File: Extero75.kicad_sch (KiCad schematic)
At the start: 314 parts, among them J1 USB_C_Receptacle_USB2.0, Q1 AO3400A, SW1 BOOT, SW2 RST, SW3 RotaryEncoder_Switch, U1 STM32F072R8Tx, U2 XC6206P332MR

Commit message: change name
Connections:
- no-connect marks 2 -> 14
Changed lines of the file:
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@@
   (no_connect (at 641.858 63.246))
   (no_connect (at 641.858 60.706))
+  (no_connect (at 716.788 174.498))
+  (no_connect (at 716.788 154.178))
+  (no_connect (at 716.788 169.418))
+  (no_connect (at 716.788 156.718))
+  (no_connect (at 716.788 166.878))
+  (no_connect (at 716.788 151.638))
+  (no_connect (at 716.788 164.338))
+  (no_connect (at 716.788 161.798))
+  (no_connect (at 716.788 159.258))
+  (no_connect (at 716.788 171.958))
+  (no_connect (at 716.788 177.038))
+  (no_connect (at 716.788 179.578))
   (wire (pts (xy 516.636 204.343) (xy 512.318 204.343))
     (stroke (width 0) (type default) (color 0 0 0 0))

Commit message: some more routing
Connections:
- net +3V3 is gone; now on net +3.3V: C12.1, C13.1, C14.1, C15.1, C16.1, C8.1, C9.1, U2.2 (VO)
- net +5V: now also Tab1.4 (LEDGND)
- net COL10: no longer U1.5 (PF0)
- net COL11: no longer U1.6 (PF1)
- net COL12: no longer U1.14 (PA0)
- net COL13: no longer U1.28 (PB2)
- net COL14: no longer U1.29 (PB10)
- net COL15: no longer U1.30 (PB11)
- net COL16: no longer U1.8 (PC0)
- net COL17: no longer U1.9 (PC1)
- net COL4: now also U1.37 (PC6); no longer U1.41 (PA8)
- net COL5: now also U1.38 (PC7); no longer U1.43 (PA10)
- net COL6: now also U1.39 (PC8); no longer U1.46 (PA13)
- net COL7: now also U1.40 (PC9); no longer U1.49 (PA14)
- net COL8: no longer U1.62 (PB9)
- net COL9: now also MX-J1.1 (COL), MX-U1.1 (COL), Num7.1 (COL); no longer U1.54 (PD2)
- net D_N: now also U1.44 (PA11); no longer U1.26 (PB0)
- net D_P: now also U1.45 (PA12); no longer U1.27 (PB1)
- net LED-: now also R21.2
- net LED_PWM: no longer U1.42 (PA9)
- net ROTA: no longer U1.4 (PC15)
- net ROTB: no longer U1.3 (PC14)
- net ROW0: now also U1.41 (PA8); no longer U1.50 (PA15)
- net ROW1: now also U1.5 (PF0); no longer U1.56 (PB4)
- net ROW2: now also U1.6 (PF1); no longer U1.57 (PB5)
- net ROW3: now also U1.8 (PC0); no longer U1.58 (PB6)
- net ROW4: now also U1.9 (PC1); no longer U1.59 (PB7)
- net ROW5: now also U1.10 (PC2); no longer U1.61 (PB8)
- net at Num1.3 (LED): now also R25.1
- net BOOT: now reaches C1.1, R3.1, SW1.2, U1.60 (BOOT0)
- net RST: now reaches C2.1, SW2.2, U1.7 (NRST)
- net UGLED: no longer names the net of U1.55 (PB3)
- no-connect marks 14 -> 4
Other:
- note removed: "RESET"
- moved on the sheet: D15, R21, R25, Tab1

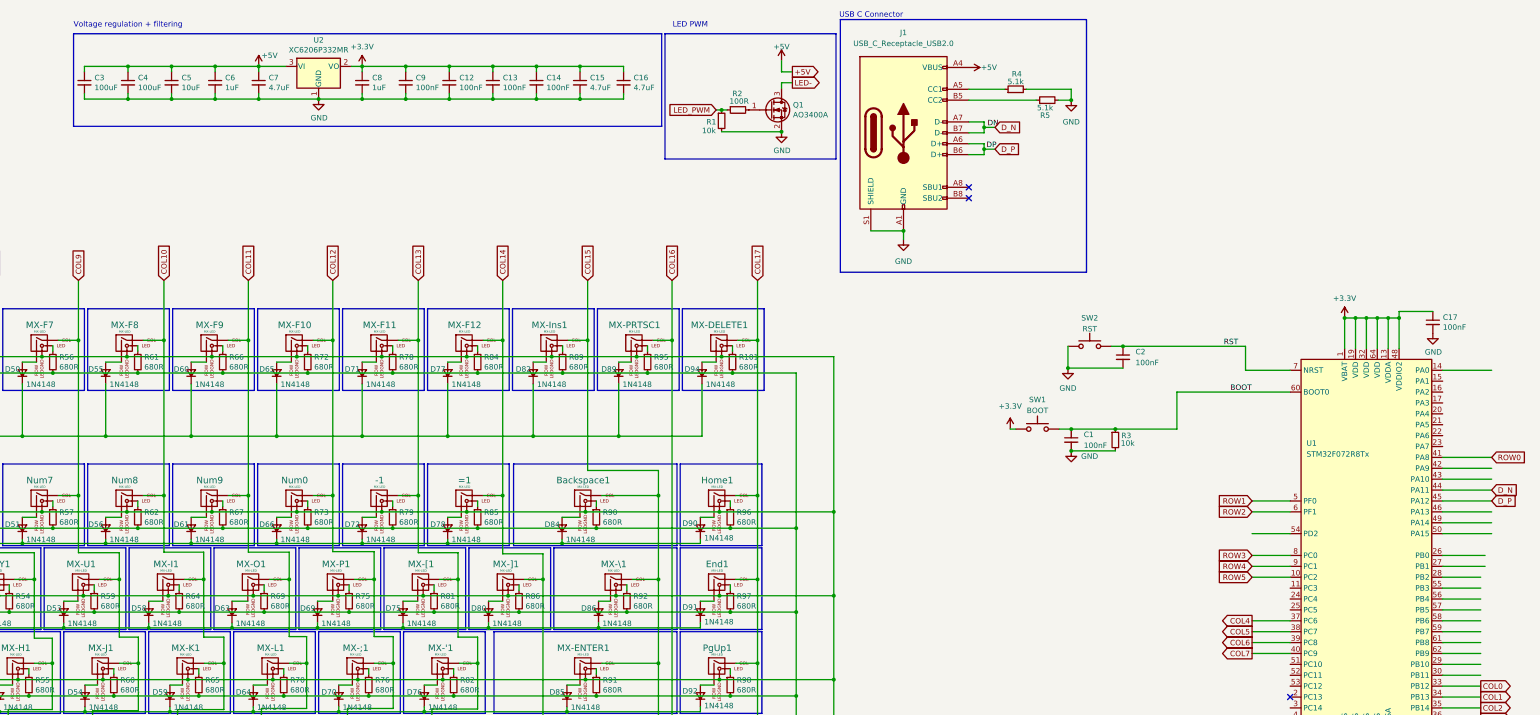
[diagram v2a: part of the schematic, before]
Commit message: Fix decoupling capacitor schematic for Voltage regulator + Some more routing
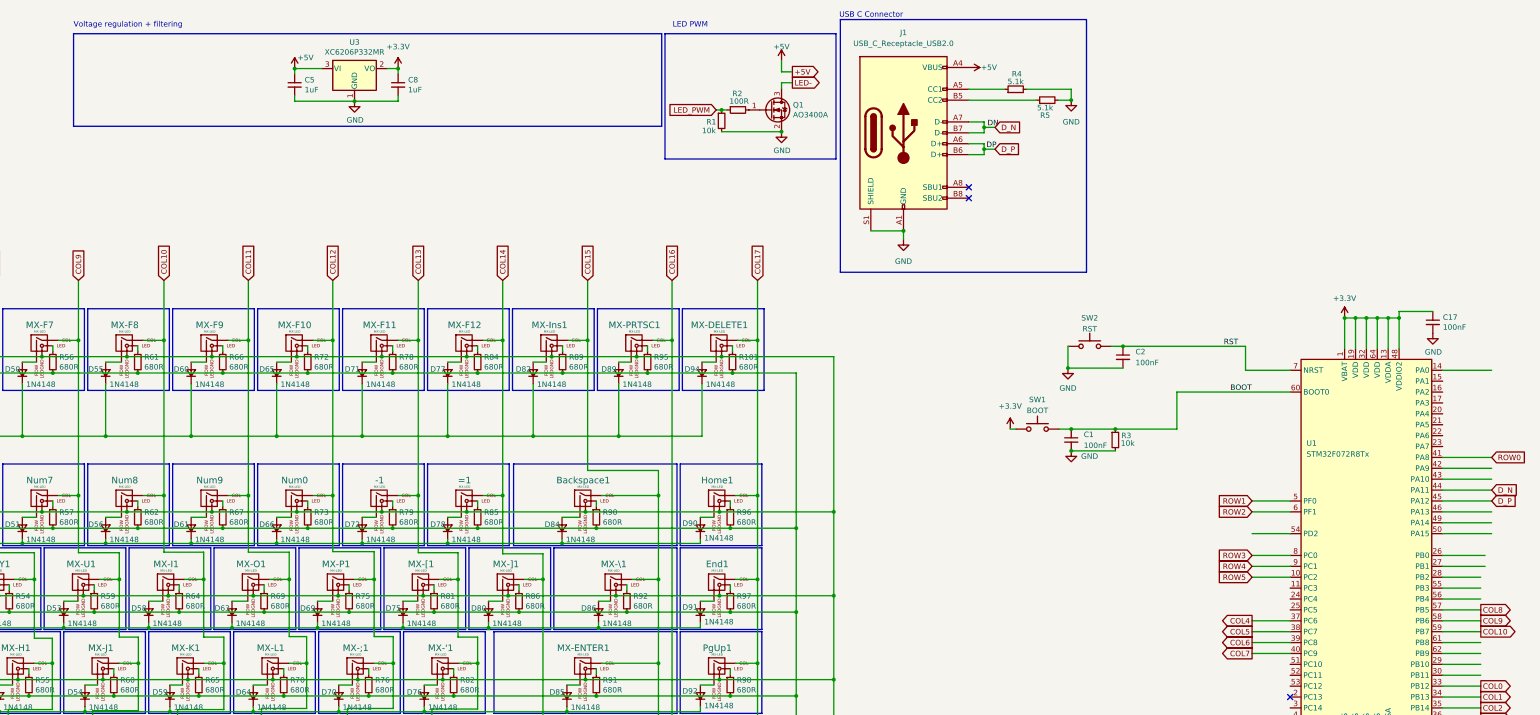
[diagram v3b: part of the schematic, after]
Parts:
- removed C12, C13, C14, C9: 100nF, Capacitor_SMD:C_0402_1005Metric, symbol Device:C_Small
- removed C15, C16, C7: 4.7uF, Capacitor_SMD:C_0402_1005Metric, symbol Device:C_Small
- removed C3, C4: 100uF, Capacitor_Tantalum_SMD:CP_EIA-3528-21_Kemet-B, symbol Device:C_Small
- removed C6: 1uF, Capacitor_SMD:C_0402_1005Metric, symbol Device:C_Small
- removed U2: XC6206P332MR, Package_TO_SOT_SMD:SOT-23, symbol isometria-75-pcb-iso-rescue:XC6206PxxxMR-Regulator_Linear-kicad-keyboard-parts
- added U3: XC6206P332MR, Package_TO_SOT_SMD:SOT-23, symbol isometria-75-pcb-iso-rescue:XC6206PxxxMR-Regulator_Linear-kicad-keyboard-parts
- C5: value 10uF -> 1uF; footprint Capacitor_Tantalum_SMD:CP_EIA-3216-18_Kemet-A -> Capacitor_SMD:C_0402_1005Metric; LCSC C7171 -> C52923
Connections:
- net +3.3V: now also U3.2 (VO)
- net +5V: now also U3.3 (VI)
- net COL10: now also U1.59 (PB7)
- net COL8: now also U1.57 (PB5)
- net COL9: now also U1.58 (PB6)
- net GND: now also U3.1 (GND)

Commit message: Rerouting + Plate + Top Case
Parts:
- removed C17: 100nF, Capacitor_SMD:C_0402_1005Metric, symbol Device:C_Small
- added C12: 1uf, Capacitor_SMD:C_0402_1005Metric, symbol Device:C_Small
- added C13: 10uf, Capacitor_SMD:C_0402_1005Metric, symbol Device:C_Small
- added C14, C3, C4, C6, C7, C9: 0,1uF, Capacitor_SMD:C_0402_1005Metric, symbol Device:C_Small
- added H1, H2, H3, H4: MountingHole, MountingHole:MountingHole_2.2mm_M2, symbol Mechanical:MountingHole
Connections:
- net +3.3V: now also C12.1, C13.1, C14.1, C3.1, C4.1, C6.1, C7.1, C9.1
- net COL11: now also U1.14 (PA0)
- net COL12: now also U1.25 (PC5)
- net COL13: now also U1.26 (PB0)
- net COL14: now also U1.27 (PB1)
- net COL15: now also U1.28 (PB2)
- net COL16: now also U1.29 (PB10)
- net COL17: now also U1.30 (PB11)
- net GND: now also C12.2, C13.2, C14.2, C3.2, C4.2, C6.2, C7.2, C9.2
- net LED_PWM: now also U1.56 (PB4)
- net ROTA: now also U1.51 (PC10)
- net ROTB: now also U1.55 (PB3)
- no-connect marks 4 -> 24
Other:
- moved on the sheet: C1, C2, C5, C8, R3, SW1, SW2, U1, U3

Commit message: Removing LED's
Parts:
- removed MX-EXTRA1: MX-LED, MX_Only:MXOnly-1U-Hotswap-LED, symbol MX_Alps_Hybrid:MX-LED
- removed Q1: AO3400A, Package_TO_SOT_SMD:SOT-23, symbol Device:Q_NMOS_GSD
- removed R1: 10k, Resistor_SMD:R_0402_1005Metric, symbol Device:R_Small
- removed R10, R100, R101, R11, R12, R13, R14, R15, R16, R17, R18, R19, R20, R21, R22, R23, R24, R25, R26, R27, R28, R29, R30, R31, R32, R33, R34, R35, R36, R37, R38, R39, R40, R41, R42, R43, R44, R45, R46, R47, R48, R49, R50, R51, R52, R53, R54, R55, R56, R57, R58, R59, R60, R61, R62, R63, R64, R65, R66, R67, R68, R69, R70, R71, R72, R73, R74, R75, R76, R77, R78, R79, R8, R80, R81, R82, R83, R84, R85, R86, R87, R88, R89, R9, R90, R91, R92, R93, R94, R95, R96, R97, R98, R99: 680R, Resistor_SMD:R_0603_1608Metric, symbol Device:R_Small
- removed R2: 100R, Resistor_SMD:R_0402_1005Metric, symbol Device:R_Small
- added EXTRA1: MX_SW_HS, marbastlib-mx:SW_MX_HS_1u, symbol marbastlib-mx:MX_SW_HS
- A1: renamed from MX-A1; footprint MX_Only:MXOnly-1U-Hotswap-LED -> marbastlib-mx:SW_MX_HS_1u; symbol MX_Alps_Hybrid:MX-LED -> marbastlib-mx:MX_SW_HS
- B1: renamed from MX-B1; footprint MX_Only:MXOnly-1U-Hotswap-LED -> marbastlib-mx:SW_MX_HS_1u; symbol MX_Alps_Hybrid:MX-LED -> marbastlib-mx:MX_SW_HS
- Backspace1: footprint MX_Only:MXOnly-2U-Hotswap-LED -> marbastlib-mx:SW_MX_HS_1u; symbol MX_Alps_Hybrid:MX-LED -> marbastlib-mx:MX_SW_HS
- C1, C10, C11, C12, C13, C14, C2, C3, C4, C6, C7, C9: footprint Capacitor_SMD:C_0402_1005Metric -> Capacitor_SMD:C_0603_1608Metric
- C5, C8: footprint Capacitor_SMD:C_0402_1005Metric -> Capacitor_SMD:C_0603_1608Metric; LCSC C52923 -> (none)
- CAPSLOCK1, RIGHTSHIFT1: footprint MX_Only:MXOnly-1.75U-Hotswap-LED -> marbastlib-mx:SW_MX_HS_1u; symbol MX_Alps_Hybrid:MX-LED -> marbastlib-mx:MX_SW_HS
- Ckey1: renamed from MX-C1; footprint MX_Only:MXOnly-1U-Hotswap-LED -> marbastlib-mx:SW_MX_HS_1u; symbol MX_Alps_Hybrid:MX-LED -> marbastlib-mx:MX_SW_HS
- CloseBracket1: renamed from MX-]1; footprint MX_Only:MXOnly-1U-Hotswap-LED -> marbastlib-mx:SW_MX_HS_1u; symbol MX_Alps_Hybrid:MX-LED -> marbastlib-mx:MX_SW_HS
- CommaSign1: renamed from MX-,1; footprint MX_Only:MXOnly-1U-Hotswap-LED -> marbastlib-mx:SW_MX_HS_1u; symbol MX_Alps_Hybrid:MX-LED -> marbastlib-mx:MX_SW_HS
- D1, D10, D11, D12, D13, D14, D15, D16, D17, D18, D19, D2, D20, D21, D22, D23, D24, D25, D26, D27, D28, D29, D3, D30, D31, D32, D33, D34, D35, D36, D37, D38, D39, D4, D40, D41, D42, D43, D44, D45, D46, D47, D48, D49, D5, D50, D51, D52, D53, D54, D55, D56, D57, D58, D59, D6, D60, D61, D62, D63, D64, D65, D66, D67, D68, D69, D7, D70, D71, D72, D73, D74, D75, D76, D77, D78, D79, D8, D80, D81, D82, D83, D84, D85, D86, D87, D88, D89, D9, D90, D91, D92, D93, D94, D95: footprint Diode_SMD:D_SOD-323F -> Diode_SMD:D_SOD-123
- DELETE1: renamed from MX-DELETE1; footprint MX_Only:MXOnly-1U-Hotswap-LED -> marbastlib-mx:SW_MX_HS_1u; symbol MX_Alps_Hybrid:MX-LED -> marbastlib-mx:MX_SW_HS
- DOWNARROW1, End1, FNKEY1, Home1, LEFTARROW1, Num0, Num1, Num2, Num3, Num4, Num5, Num6, Num7, Num8, Num9, PgDn1, PgUp1, RIGHTALT1, RIGHTARROW1, RIGHTCONTROL1, UPARROW1: footprint MX_Only:MXOnly-1U-Hotswap-LED -> marbastlib-mx:SW_MX_HS_1u; symbol MX_Alps_Hybrid:MX-LED -> marbastlib-mx:MX_SW_HS
- Dkey1: renamed from MX-D1; footprint MX_Only:MXOnly-1U-Hotswap-LED -> marbastlib-mx:SW_MX_HS_1u; symbol MX_Alps_Hybrid:MX-LED -> marbastlib-mx:MX_SW_HS
- DotSign1: renamed from MX-.1; footprint MX_Only:MXOnly-1U-Hotswap-LED -> marbastlib-mx:SW_MX_HS_1u; symbol MX_Alps_Hybrid:MX-LED -> marbastlib-mx:MX_SW_HS
- E1: renamed from MX-E1; footprint MX_Only:MXOnly-1U-Hotswap-LED -> marbastlib-mx:SW_MX_HS_1u; symbol MX_Alps_Hybrid:MX-LED -> marbastlib-mx:MX_SW_HS
- ENTER1: renamed from MX-ENTER1; footprint MX_Only:MXOnly-2.25U-Hotswap-LED -> marbastlib-mx:SW_MX_HS_1u; symbol MX_Alps_Hybrid:MX-LED -> marbastlib-mx:MX_SW_HS
- ESC1: renamed from MX-ESC1; footprint MX_Only:MXOnly-1U-Hotswap-LED -> marbastlib-mx:SW_MX_HS_1u; symbol MX_Alps_Hybrid:MX-LED -> marbastlib-mx:MX_SW_HS
- EXTRA10: renamed from MX-EXTRA10; footprint MX_Only:MXOnly-1U-Hotswap-LED -> marbastlib-mx:SW_MX_HS_1u; symbol MX_Alps_Hybrid:MX-LED -> marbastlib-mx:MX_SW_HS
- EXTRA2: renamed from MX-EXTRA2; footprint MX_Only:MXOnly-1U-Hotswap-LED -> marbastlib-mx:SW_MX_HS_1u; symbol MX_Alps_Hybrid:MX-LED -> marbastlib-mx:MX_SW_HS
- EXTRA3: renamed from MX-EXTRA3; footprint MX_Only:MXOnly-1U-Hotswap-LED -> marbastlib-mx:SW_MX_HS_1u; symbol MX_Alps_Hybrid:MX-LED -> marbastlib-mx:MX_SW_HS
- EXTRA4: renamed from MX-EXTRA4; footprint MX_Only:MXOnly-1U-Hotswap-LED -> marbastlib-mx:SW_MX_HS_1u; symbol MX_Alps_Hybrid:MX-LED -> marbastlib-mx:MX_SW_HS
- EXTRA5: renamed from MX-EXTRA5; footprint MX_Only:MXOnly-1U-Hotswap-LED -> marbastlib-mx:SW_MX_HS_1u; symbol MX_Alps_Hybrid:MX-LED -> marbastlib-mx:MX_SW_HS
- EXTRA6: renamed from MX-EXTRA6; footprint MX_Only:MXOnly-1U-Hotswap-LED -> marbastlib-mx:SW_MX_HS_1u; symbol MX_Alps_Hybrid:MX-LED -> marbastlib-mx:MX_SW_HS
- EXTRA7: renamed from MX-EXTRA7; footprint MX_Only:MXOnly-1U-Hotswap-LED -> marbastlib-mx:SW_MX_HS_1u; symbol MX_Alps_Hybrid:MX-LED -> marbastlib-mx:MX_SW_HS
- EXTRA8: renamed from MX-EXTRA8; footprint MX_Only:MXOnly-1U-Hotswap-LED -> marbastlib-mx:SW_MX_HS_1u; symbol MX_Alps_Hybrid:MX-LED -> marbastlib-mx:MX_SW_HS
- EXTRA9: renamed from MX-EXTRA9; footprint MX_Only:MXOnly-1U-Hotswap-LED -> marbastlib-mx:SW_MX_HS_1u; symbol MX_Alps_Hybrid:MX-LED -> marbastlib-mx:MX_SW_HS
- EqualSign1: renamed from =1; footprint MX_Only:MXOnly-1U-Hotswap-LED -> marbastlib-mx:SW_MX_HS_1u; symbol MX_Alps_Hybrid:MX-LED -> marbastlib-mx:MX_SW_HS
- F1: renamed from MX-F1; footprint MX_Only:MXOnly-1U-Hotswap-LED -> marbastlib-mx:SW_MX_HS_1u; symbol MX_Alps_Hybrid:MX-LED -> marbastlib-mx:MX_SW_HS
- F10: renamed from MX-F10; footprint MX_Only:MXOnly-1U-Hotswap-LED -> marbastlib-mx:SW_MX_HS_1u; symbol MX_Alps_Hybrid:MX-LED -> marbastlib-mx:MX_SW_HS
- F11: renamed from MX-F11; footprint MX_Only:MXOnly-1U-Hotswap-LED -> marbastlib-mx:SW_MX_HS_1u; symbol MX_Alps_Hybrid:MX-LED -> marbastlib-mx:MX_SW_HS
- F12: renamed from MX-F12; footprint MX_Only:MXOnly-1U-Hotswap-LED -> marbastlib-mx:SW_MX_HS_1u; symbol MX_Alps_Hybrid:MX-LED -> marbastlib-mx:MX_SW_HS
- F2: renamed from MX-F2; footprint MX_Only:MXOnly-1U-Hotswap-LED -> marbastlib-mx:SW_MX_HS_1u; symbol MX_Alps_Hybrid:MX-LED -> marbastlib-mx:MX_SW_HS
- F3: renamed from MX-F3; footprint MX_Only:MXOnly-1U-Hotswap-LED -> marbastlib-mx:SW_MX_HS_1u; symbol MX_Alps_Hybrid:MX-LED -> marbastlib-mx:MX_SW_HS
- F4: renamed from MX-F4; footprint MX_Only:MXOnly-1U-Hotswap-LED -> marbastlib-mx:SW_MX_HS_1u; symbol MX_Alps_Hybrid:MX-LED -> marbastlib-mx:MX_SW_HS
- F5: renamed from MX-F5; footprint MX_Only:MXOnly-1U-Hotswap-LED -> marbastlib-mx:SW_MX_HS_1u; symbol MX_Alps_Hybrid:MX-LED -> marbastlib-mx:MX_SW_HS
- F6: renamed from MX-F6; footprint MX_Only:MXOnly-1U-Hotswap-LED -> marbastlib-mx:SW_MX_HS_1u; symbol MX_Alps_Hybrid:MX-LED -> marbastlib-mx:MX_SW_HS
- F7: renamed from MX-F7; footprint MX_Only:MXOnly-1U-Hotswap-LED -> marbastlib-mx:SW_MX_HS_1u; symbol MX_Alps_Hybrid:MX-LED -> marbastlib-mx:MX_SW_HS
- F8: renamed from MX-F8; footprint MX_Only:MXOnly-1U-Hotswap-LED -> marbastlib-mx:SW_MX_HS_1u; symbol MX_Alps_Hybrid:MX-LED -> marbastlib-mx:MX_SW_HS
- F9: renamed from MX-F9; footprint MX_Only:MXOnly-1U-Hotswap-LED -> marbastlib-mx:SW_MX_HS_1u; symbol MX_Alps_Hybrid:MX-LED -> marbastlib-mx:MX_SW_HS
- Fkey1: renamed from MX-Fkey1; footprint MX_Only:MXOnly-1U-Hotswap-LED -> marbastlib-mx:SW_MX_HS_1u; symbol MX_Alps_Hybrid:MX-LED -> marbastlib-mx:MX_SW_HS
- G1: renamed from MX-G1; footprint MX_Only:MXOnly-1U-Hotswap-LED -> marbastlib-mx:SW_MX_HS_1u; symbol MX_Alps_Hybrid:MX-LED -> marbastlib-mx:MX_SW_HS
- Hkey1: renamed from MX-H1; footprint MX_Only:MXOnly-1U-Hotswap-LED -> marbastlib-mx:SW_MX_HS_1u; symbol MX_Alps_Hybrid:MX-LED -> marbastlib-mx:MX_SW_HS
- I1: renamed from MX-I1; footprint MX_Only:MXOnly-1U-Hotswap-LED -> marbastlib-mx:SW_MX_HS_1u; symbol MX_Alps_Hybrid:MX-LED -> marbastlib-mx:MX_SW_HS
- Ins1: renamed from MX-Ins1; footprint MX_Only:MXOnly-1U-Hotswap-LED -> marbastlib-mx:SW_MX_HS_1u; symbol MX_Alps_Hybrid:MX-LED -> marbastlib-mx:MX_SW_HS
- J1: footprint Connector_USB:USB_C_Receptacle_GCT_USB4085 -> Connector_USB:USB_C_Receptacle_GCT_USB4105-xx-A_16P_TopMnt_Horizontal
- Jkey1: renamed from MX-J1; footprint MX_Only:MXOnly-1U-Hotswap-LED -> marbastlib-mx:SW_MX_HS_1u; symbol MX_Alps_Hybrid:MX-LED -> marbastlib-mx:MX_SW_HS
- K1: renamed from MX-K1; footprint MX_Only:MXOnly-1U-Hotswap-LED -> marbastlib-mx:SW_MX_HS_1u; symbol MX_Alps_Hybrid:MX-LED -> marbastlib-mx:MX_SW_HS
- L1: renamed from MX-L1; footprint MX_Only:MXOnly-1U-Hotswap-LED -> marbastlib-mx:SW_MX_HS_1u; symbol MX_Alps_Hybrid:MX-LED -> marbastlib-mx:MX_SW_HS
- LEFTALT1, LEFTCTRL1, WINDOWSKEY1: footprint MX_Only:MXOnly-1.25U-Hotswap-LED -> marbastlib-mx:SW_MX_HS_1u; symbol MX_Alps_Hybrid:MX-LED -> marbastlib-mx:MX_SW_HS
- LEFTSHIFT1: footprint MX_Only:MXOnly-2.25U-Hotswap-LED -> marbastlib-mx:SW_MX_HS_1u; symbol MX_Alps_Hybrid:MX-LED -> marbastlib-mx:MX_SW_HS
- M1: renamed from MX-M1; footprint MX_Only:MXOnly-1U-Hotswap-LED -> marbastlib-mx:SW_MX_HS_1u; symbol MX_Alps_Hybrid:MX-LED -> marbastlib-mx:MX_SW_HS
- Matilda1: renamed from MX-`1; footprint MX_Only:MXOnly-1U-Hotswap-LED -> marbastlib-mx:SW_MX_HS_1u; symbol MX_Alps_Hybrid:MX-LED -> marbastlib-mx:MX_SW_HS
- MinusSign1: renamed from -1; footprint MX_Only:MXOnly-1U-Hotswap-LED -> marbastlib-mx:SW_MX_HS_1u; symbol MX_Alps_Hybrid:MX-LED -> marbastlib-mx:MX_SW_HS
- N1: renamed from MX-N1; footprint MX_Only:MXOnly-1U-Hotswap-LED -> marbastlib-mx:SW_MX_HS_1u; symbol MX_Alps_Hybrid:MX-LED -> marbastlib-mx:MX_SW_HS
- O1: renamed from MX-O1; footprint MX_Only:MXOnly-1U-Hotswap-LED -> marbastlib-mx:SW_MX_HS_1u; symbol MX_Alps_Hybrid:MX-LED -> marbastlib-mx:MX_SW_HS
- OpenBracket1: renamed from MX-[1; footprint MX_Only:MXOnly-1U-Hotswap-LED -> marbastlib-mx:SW_MX_HS_1u; symbol MX_Alps_Hybrid:MX-LED -> marbastlib-mx:MX_SW_HS
- P1: renamed from MX-P1; footprint MX_Only:MXOnly-1U-Hotswap-LED -> marbastlib-mx:SW_MX_HS_1u; symbol MX_Alps_Hybrid:MX-LED -> marbastlib-mx:MX_SW_HS
- PRTSC1: renamed from MX-PRTSC1; footprint MX_Only:MXOnly-1U-Hotswap-LED -> marbastlib-mx:SW_MX_HS_1u; symbol MX_Alps_Hybrid:MX-LED -> marbastlib-mx:MX_SW_HS
- Q1: renamed from MX-Q1; footprint MX_Only:MXOnly-1U-Hotswap-LED -> marbastlib-mx:SW_MX_HS_1u; symbol MX_Alps_Hybrid:MX-LED -> marbastlib-mx:MX_SW_HS
- QuestionMark1: renamed from MX-/1; footprint MX_Only:MXOnly-1U-Hotswap-LED -> marbastlib-mx:SW_MX_HS_1u; symbol MX_Alps_Hybrid:MX-LED -> marbastlib-mx:MX_SW_HS
- Quote1: renamed from MX-'1; footprint MX_Only:MXOnly-1U-Hotswap-LED -> marbastlib-mx:SW_MX_HS_1u; symbol MX_Alps_Hybrid:MX-LED -> marbastlib-mx:MX_SW_HS
- R1: renamed from MX-R1; footprint MX_Only:MXOnly-1U-Hotswap-LED -> marbastlib-mx:SW_MX_HS_1u; symbol MX_Alps_Hybrid:MX-LED -> marbastlib-mx:MX_SW_HS
- R3, R6, R7: footprint Resistor_SMD:R_0402_1005Metric -> Resistor_SMD:R_0603_1608Metric
- S1: renamed from MX-S1; footprint MX_Only:MXOnly-1U-Hotswap-LED -> marbastlib-mx:SW_MX_HS_1u; symbol MX_Alps_Hybrid:MX-LED -> marbastlib-mx:MX_SW_HS
- SPACEBAR1: footprint MX_Only:MXOnly-6.25U-Hotswap-LED -> marbastlib-mx:SW_MX_HS_1u; symbol MX_Alps_Hybrid:MX-LED -> marbastlib-mx:MX_SW_HS
- Semicolon1: renamed from MX-;1; footprint MX_Only:MXOnly-1U-Hotswap-LED -> marbastlib-mx:SW_MX_HS_1u; symbol MX_Alps_Hybrid:MX-LED -> marbastlib-mx:MX_SW_HS
- Slash1: renamed from MX-\1; footprint MX_Only:MXOnly-1.5U-Hotswap-LED -> marbastlib-mx:SW_MX_HS_1u; symbol MX_Alps_Hybrid:MX-LED -> marbastlib-mx:MX_SW_HS
- T1: renamed from MX-T1; footprint MX_Only:MXOnly-1U-Hotswap-LED -> marbastlib-mx:SW_MX_HS_1u; symbol MX_Alps_Hybrid:MX-LED -> marbastlib-mx:MX_SW_HS
- Tab1: footprint MX_Only:MXOnly-1.5U-Hotswap-LED -> marbastlib-mx:SW_MX_HS_1u; symbol MX_Alps_Hybrid:MX-LED -> marbastlib-mx:MX_SW_HS
- U2: renamed from MX-U1; footprint MX_Only:MXOnly-1U-Hotswap-LED -> marbastlib-mx:SW_MX_HS_1u; symbol MX_Alps_Hybrid:MX-LED -> marbastlib-mx:MX_SW_HS
- U3: LCSC C5446 -> (none)
- V1: renamed from MX-V1; footprint MX_Only:MXOnly-1U-Hotswap-LED -> marbastlib-mx:SW_MX_HS_1u; symbol MX_Alps_Hybrid:MX-LED -> marbastlib-mx:MX_SW_HS
- W1: renamed from MX-W1; footprint MX_Only:MXOnly-1U-Hotswap-LED -> marbastlib-mx:SW_MX_HS_1u; symbol MX_Alps_Hybrid:MX-LED -> marbastlib-mx:MX_SW_HS
- X1: renamed from MX-X1; footprint MX_Only:MXOnly-1U-Hotswap-LED -> marbastlib-mx:SW_MX_HS_1u; symbol MX_Alps_Hybrid:MX-LED -> marbastlib-mx:MX_SW_HS
- Y1: renamed from MX-Y1; footprint MX_Only:MXOnly-1U-Hotswap-LED -> marbastlib-mx:SW_MX_HS_1u; symbol MX_Alps_Hybrid:MX-LED -> marbastlib-mx:MX_SW_HS
- Z1: renamed from MX-Z1; footprint MX_Only:MXOnly-1U-Hotswap-LED -> marbastlib-mx:SW_MX_HS_1u; symbol MX_Alps_Hybrid:MX-LED -> marbastlib-mx:MX_SW_HS
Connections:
- net +5V: no longer A1.4 (LEDGND), B1.4 (LEDGND), Backspace1.4 (LEDGND), CAPSLOCK1.4 (LEDGND), Ckey1.4 (LEDGND), CloseBracket1.4 (LEDGND), CommaSign1.4 (LEDGND), DELETE1.4 (LEDGND), DOWNARROW1.4 (LEDGND), Dkey1.4 (LEDGND), DotSign1.4 (LEDGND), E1.4 (LEDGND), ENTER1.4 (LEDGND), ESC1.4 (LEDGND), EXTRA10.4 (LEDGND), EXTRA2.4 (LEDGND), EXTRA3.4 (LEDGND), EXTRA4.4 (LEDGND), EXTRA5.4 (LEDGND), EXTRA6.4 (LEDGND), EXTRA7.4 (LEDGND), EXTRA8.4 (LEDGND), EXTRA9.4 (LEDGND), End1.4 (LEDGND), EqualSign1.4 (LEDGND), F1.4 (LEDGND), F10.4 (LEDGND), F11.4 (LEDGND), F12.4 (LEDGND), F2.4 (LEDGND), F3.4 (LEDGND), F4.4 (LEDGND), F5.4 (LEDGND), F6.4 (LEDGND), F7.4 (LEDGND), F8.4 (LEDGND), F9.4 (LEDGND), FNKEY1.4 (LEDGND), Fkey1.4 (LEDGND), G1.4 (LEDGND), Hkey1.4 (LEDGND), Home1.4 (LEDGND), I1.4 (LEDGND), Ins1.4 (LEDGND), Jkey1.4 (LEDGND), K1.4 (LEDGND), L1.4 (LEDGND), LEFTALT1.4 (LEDGND), LEFTARROW1.4 (LEDGND), LEFTCTRL1.4 (LEDGND), LEFTSHIFT1.4 (LEDGND), M1.4 (LEDGND), Matilda1.4 (LEDGND), MinusSign1.4 (LEDGND), N1.4 (LEDGND), Num0.4 (LEDGND), Num1.4 (LEDGND), Num2.4 (LEDGND), Num3.4 (LEDGND), Num4.4 (LEDGND), Num5.4 (LEDGND), Num6.4 (LEDGND), Num7.4 (LEDGND), Num8.4 (LEDGND), Num9.4 (LEDGND), O1.4 (LEDGND), OpenBracket1.4 (LEDGND), P1.4 (LEDGND), PRTSC1.4 (LEDGND), PgDn1.4 (LEDGND), PgUp1.4 (LEDGND), Q1.4 (LEDGND), QuestionMark1.4 (LEDGND), Quote1.4 (LEDGND), R1.4 (LEDGND), RIGHTALT1.4 (LEDGND), RIGHTARROW1.4 (LEDGND), RIGHTCONTROL1.4 (LEDGND), RIGHTSHIFT1.4 (LEDGND), S1.4 (LEDGND), SPACEBAR1.4 (LEDGND), Semicolon1.4 (LEDGND), Slash1.4 (LEDGND), T1.4 (LEDGND), Tab1.4 (LEDGND), U2.4 (LEDGND), UPARROW1.4 (LEDGND), V1.4 (LEDGND), W1.4 (LEDGND), WINDOWSKEY1.4 (LEDGND), X1.4 (LEDGND), Y1.4 (LEDGND), Z1.4 (LEDGND)
- net COL0: now also EXTRA1.1
- net COL13: no longer Quote1.1 (COL)
- net COL16: no longer DOWNARROW1.1 (COL)
- net at D1.2 (A): now also EXTRA1.2
- net at Quote1.2: no longer D76.2 (A)
- net at D88.2 (A): no longer DOWNARROW1.2 (ROW)
- net LED_PWM: no longer names the net of U1.56 (PB4)
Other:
- note removed: "LED PWM"
- moved on the sheet: C5, C8, U3

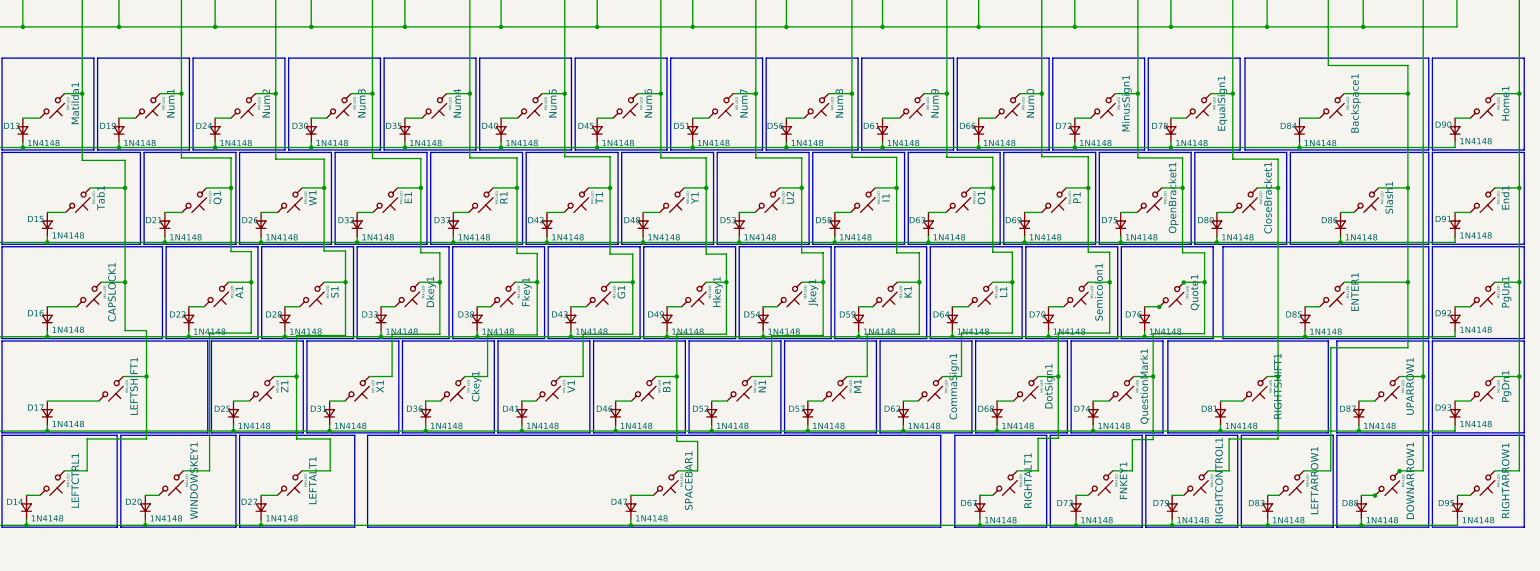
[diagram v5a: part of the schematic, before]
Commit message: Changing footprints
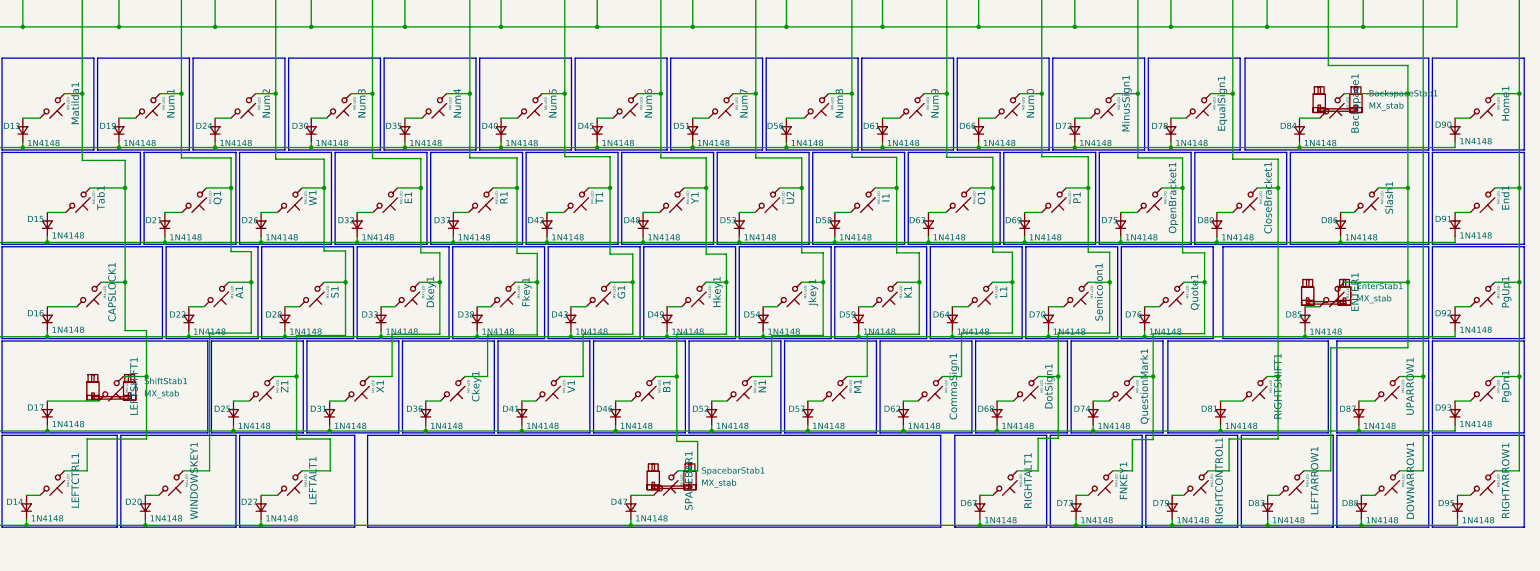
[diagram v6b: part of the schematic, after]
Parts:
- added BackspaceStab1: MX_stab, marbastlib-mx:STAB_MX_P_2u, symbol marbastlib-mx:MX_stab
- added EnterStab1, ShiftStab1: MX_stab, marbastlib-mx:STAB_MX_P_2.25u, symbol marbastlib-mx:MX_stab
- added SpacebarStab1: MX_stab, marbastlib-mx:STAB_MX_P_6.25u, symbol marbastlib-mx:MX_stab
- CAPSLOCK1, RIGHTSHIFT1: footprint marbastlib-mx:SW_MX_HS_1u -> marbastlib-mx:SW_MX_HS_1.75u
- LEFTALT1, LEFTCTRL1, WINDOWSKEY1: footprint marbastlib-mx:SW_MX_HS_1u -> marbastlib-mx:SW_MX_HS_1.25u
- Slash1, Tab1: footprint marbastlib-mx:SW_MX_HS_1u -> marbastlib-mx:SW_MX_HS_1.5u
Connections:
- net COL13: now also Quote1.1
- net COL16: now also DOWNARROW1.1
- net at Quote1.2: now also D76.2 (A)
- net at D88.2 (A): now also DOWNARROW1.2
